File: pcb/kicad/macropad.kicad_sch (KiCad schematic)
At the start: 18 parts, among them J1 OLED_128x32, J3 01x01_Pin, SW1 RESET_Push, U1 5-Way Nav

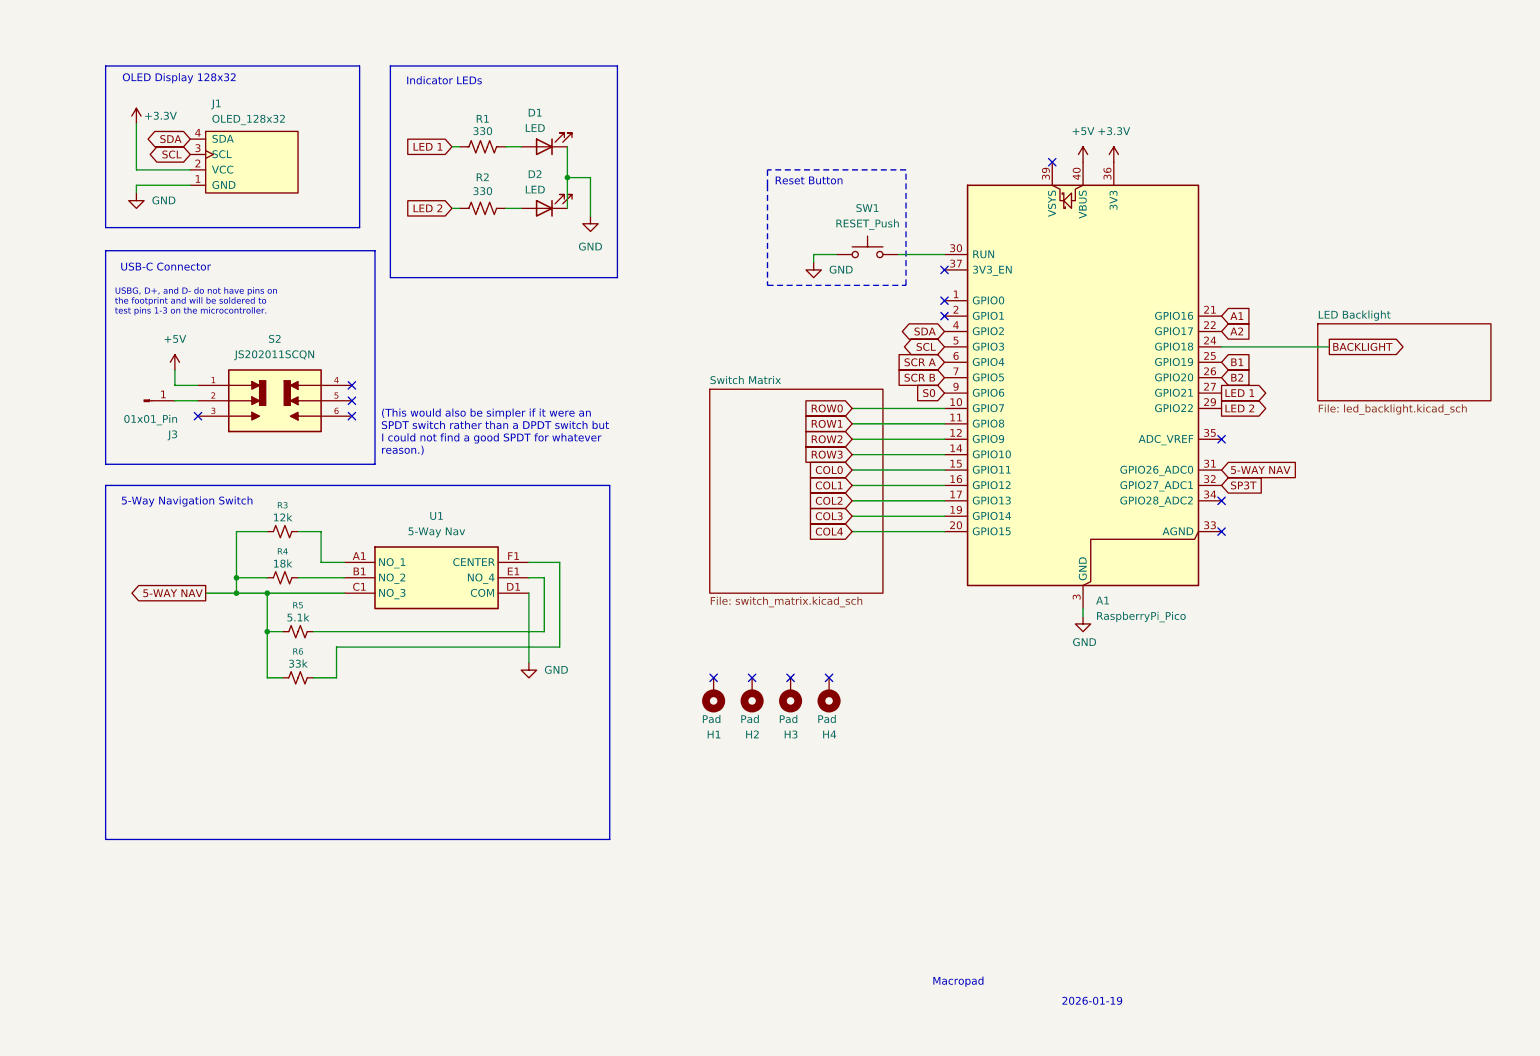
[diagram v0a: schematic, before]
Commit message: Simplified pcb; now fits within 10x10cm
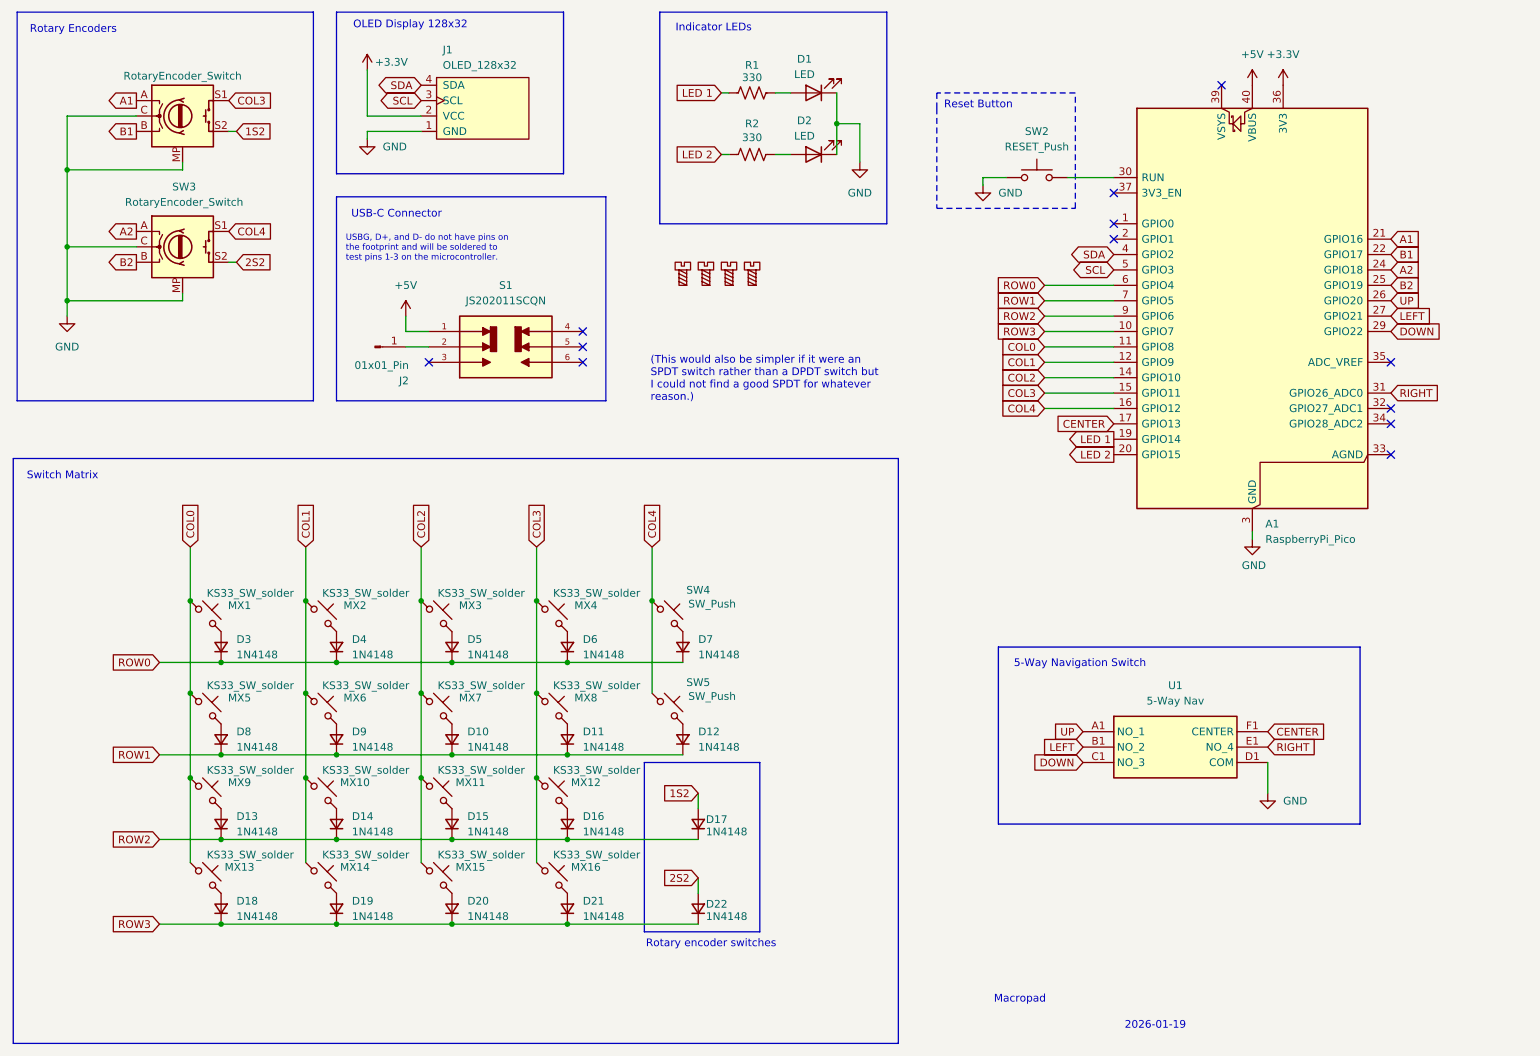
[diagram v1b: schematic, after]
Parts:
- removed H1, H2, H3, H4: Pad, MountingHole:MountingHole_2.2mm_M2_Pad, symbol Mechanical:MountingHole_Pad
- removed R3: 12k, Resistor_THT:R_Axial_DIN0207_L6.3mm_D2.5mm_P10.16mm_Horizontal, symbol Device:R_Small_US
- removed R4: 18k, Resistor_THT:R_Axial_DIN0207_L6.3mm_D2.5mm_P10.16mm_Horizontal, symbol Device:R_Small_US
- removed R5: 5.1k, Resistor_THT:R_Axial_DIN0207_L6.3mm_D2.5mm_P10.16mm_Horizontal, symbol Device:R_Small_US
- removed R6: 33k, Resistor_THT:R_Axial_DIN0207_L6.3mm_D2.5mm_P10.16mm_Horizontal, symbol Device:R_Small_US
- added D10, D11, D12, D13, D14, D15, D16, D17, D18, D19, D20, D21, D22, D3, D4, D5, D6, D7, D8, D9: 1N4148, macropad_components:Diode_DO-35, symbol Device:D_Small
- added H1, H2, H3, H4: MountingScrew, MountingHole:MountingHole_2.2mm_M2, symbol Auxiliary_Items:MountingScrew
- added MX1, MX10, MX11, MX12, MX15, MX16, MX2, MX3, MX4, MX5, MX6, MX7, MX8, MX9: KS33_SW_solder, Button_Switch_Keyboard:SW_Cherry_MX_1.00u_PCB, symbol Switch:SW_Push_45deg
- added MX13, MX14: KS33_SW_solder, Button_Switch_Keyboard:SW_Cherry_MX_1.50u_PCB, symbol Switch:SW_Push_45deg
- added SW1, SW3: RotaryEncoder_Switch, Rotary_Encoder:RotaryEncoder_Alps_EC11E-Switch_Vertical_H20mm, symbol Device:RotaryEncoder_Switch_MP
- added SW4, SW5: SW_Push, Button_Switch_THT:SW_PUSH_6mm_H7.3mm, symbol Switch:SW_Push_45deg
- J1: footprint Connector_PinHeader_2.54mm:PinHeader_1x04_P2.54mm_Vertical -> macropad_components:OLED_128x32
- renumbered J3 to J2, S2 to S1, SW1 to SW2
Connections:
- net BACKLIGHT is gone; now on net A2: A1.24 (GPIO18)
- net S0 is gone; now on net ROW2: A1.9 (GPIO6)
- net SCR A is gone; now on net ROW0: A1.6 (GPIO4)
- net SCR B is gone; now on net ROW1: A1.7 (GPIO5)
- net A1: now also SW1.A
- net A2: now also SW3.A; no longer A1.22 (GPIO17)
- net B1: now also A1.22 (GPIO17), SW1.B; no longer A1.25 (GPIO19)
- net B2: now also A1.25 (GPIO19), SW3.B; no longer A1.26 (GPIO20)
- net COL0: now also A1.11 (GPIO8), MX1.1, MX13.1, MX5.1, MX9.1; no longer A1.15 (GPIO11)
- net COL1: now also A1.12 (GPIO9), MX10.1, MX14.1, MX2.1, MX6.1; no longer A1.16 (GPIO12)
- net COL2: now also A1.14 (GPIO10), MX11.1, MX15.1, MX3.1, MX7.1; no longer A1.17 (GPIO13)
- net COL3: now also A1.15 (GPIO11), MX12.1, MX16.1, MX4.1, MX8.1, SW1.S1; no longer A1.19 (GPIO14)
- net COL4: now also A1.16 (GPIO12), SW3.S1, SW4.1, SW5.1; no longer A1.20 (GPIO15)
- net GND: now also SW1.C, SW1.MP, SW3.C, SW3.MP
- net LED 1: now also A1.19 (GPIO14); no longer A1.27 (GPIO21)
- net LED 2: now also A1.20 (GPIO15); no longer A1.29 (GPIO22)
- net ROW0: now also D3.1 (K), D4.1 (K), D5.1 (K), D6.1 (K), D7.1 (K); no longer A1.10 (GPIO7)
- net ROW1: now also D10.1 (K), D11.1 (K), D12.1 (K), D8.1 (K), D9.1 (K); no longer A1.11 (GPIO8)
- net ROW2: now also D13.1 (K), D14.1 (K), D15.1 (K), D16.1 (K), D17.1 (K); no longer A1.12 (GPIO9)
- net ROW3: now also A1.10 (GPIO7), D18.1 (K), D19.1 (K), D20.1 (K), D21.1 (K), D22.1 (K); no longer A1.14 (GPIO10)
- net LEFT: now reaches U1.B1 (NO_2)
- net LEFT: now also A1.27 (GPIO21)
- net CENTER: now reaches U1.F1 (CENTER)
- net CENTER: now also A1.17 (GPIO13)
- net UP: now reaches U1.A1 (NO_1)
- net UP: now also A1.26 (GPIO20)
- net RIGHT: now reaches U1.E1 (NO_4)
- net RIGHT: now also A1.31 (GPIO26_ADC0)
- net 5-WAY NAV renamed DOWN
- net DOWN: now also A1.29 (GPIO22); no longer A1.31 (GPIO26_ADC0)
- net SP3T: no longer names the net of A1.32 (GPIO27_ADC1)
- new net: D19.2 (A), MX14.2
- new net: D16.2 (A), MX12.2
- new net: D12.2 (A), SW5.2
- new net: D5.2 (A), MX3.2
- new net: D3.2 (A), MX1.2
- new net: D14.2 (A), MX10.2
- new net: D20.2 (A), MX15.2
- new net: D21.2 (A), MX16.2
- new net: D13.2 (A), MX9.2
- new net: D11.2 (A), MX8.2
- new net: D4.2 (A), MX2.2
- new net: D7.2 (A), SW4.2
- new net: D9.2 (A), MX6.2
- new net: D10.2 (A), MX7.2
- new net: D6.2 (A), MX4.2
- new net: D18.2 (A), MX13.2
- new net: D15.2 (A), MX11.2
- new net: D8.2 (A), MX5.2
- new net 1S2: D17.2 (A), SW1.S2
- new net 2S2: D22.2 (A), SW3.S2
- no-connect marks 15 -> 12
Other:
- removed sheet LED Backlight
- removed sheet Switch Matrix
- note added: "Rotary Encoders"
- note added: "Rotary encoder switches"
- note added: "Switch Matrix"
- moved on the sheet: A1, D1, D2, J1, J2, R1, R2, S1, SW2, U1
